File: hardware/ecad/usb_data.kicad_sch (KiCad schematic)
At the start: 0 parts

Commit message: finsihed 6/7 sheets, usb_data needs work. Some warnings to be dealt with aswell but no hard errors.
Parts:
- added C19: 100nF, Capacitor_SMD:C_01005_0402Metric, symbol Device:C
- added U6: TS3USB30EDGSR, Package_SO:TSSOP-10_3x3mm_P0.5mm, symbol Interface_USB:TS3USB30EDGSR
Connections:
- new net GND: C19.2, U6.5 (GND)
- new net MODE_SEL: U6.1 (S), U6.9 (~{OE})
- new net SYS_3V3: C19.1, U6.10 (VCC)
- new net USB_D+_ESP: U6.2 (D1+)
- new net USB_D+_KBD: U6.4 (D+)
- new net USB_D+_UP: U6.3 (D2+)
- new net USB_D-_ESP: U6.8 (D1-)
- new net USB_D-_KBD: U6.6 (D-)
- new net USB_D-_UP: U6.7 (D2-)
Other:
- company: (none) -> āvega sytems

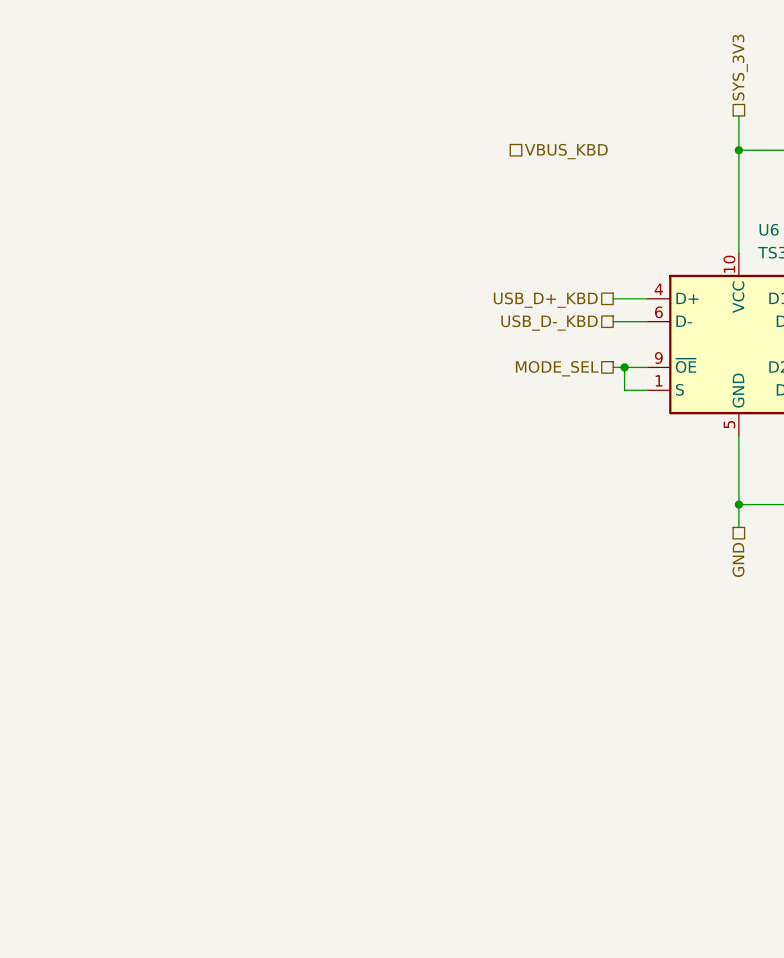
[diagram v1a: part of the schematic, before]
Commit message: feat: complete schematic design for midi2BLE v1
- Add 7-sheet hierarchical schematic covering full system architecture
- Power sheet: BQ24079RGTT charger, TPS62162DSG 3.3V buck, TLV61047DDC
  5V boost, PRTR5V0U2X ESD protection, USB-C receptacle with CC resistors
- ESP32-S3 sheet: WROOM-1-N8R2 module, UART header, boot/reset buttons,
  MODE_SEL debounce circuit, BAT_SENSE ADC input
- OLED UI sheet: SPI SSD1306 connector (GPIO35/36/10/9/8)
- Battery sense sheet: resistor divider for ADC1 battery voltage monitoring
- VBUS switching sheet: TPS2116DRL power mux for BOOST_5V/VBUS_IN selection
- USB data sheet: TS3USB30EDGSR USB 2.0 mux, keyboard USB-B connector,
  PRTR5V0U2X ESD protection on keyboard data lines
- Fix OLED from I2C to SPI, reassign GPIO11/12 away from octal flash
- Fix BQ24079 TS pin from VBUS_IN to 10k resistor to GND
- Set ISET=590R (1.5A charge), ILIM=1k (1.55A input limit) for 2500-3000mAh LiPo
- Pass ERC with 0 errors, 0 warnings (6 ignored: BQ24079 symbol quirks)
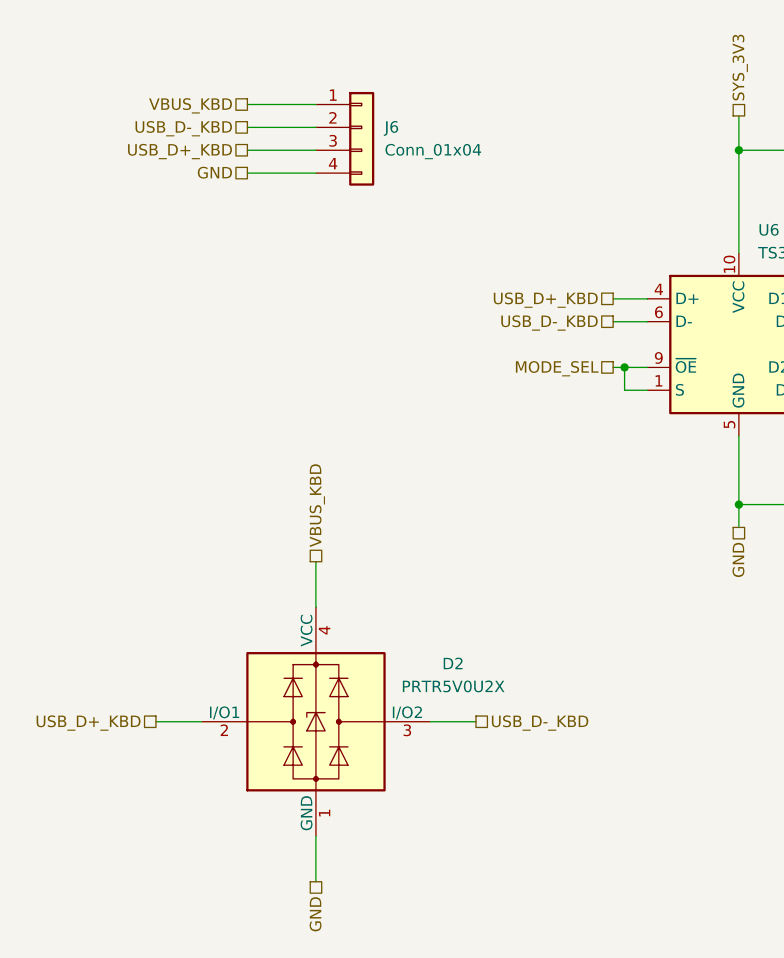
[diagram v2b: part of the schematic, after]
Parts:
- added D2: PRTR5V0U2X, Package_TO_SOT_SMD:SOT-143, symbol Power_Protection:PRTR5V0U2X
- added J6: Conn_01x04, Connector_JST:JST_PH_B4B-PH-K_1x04_P2.00mm_Vertical, symbol Connector_Generic:Conn_01x04
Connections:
- net GND: now also D2.1 (GND), J6.4 (Pin_4)
- net USB_D+_KBD: now also D2.2 (I/O1), J6.3 (Pin_3)
- net USB_D-_KBD: now also D2.3 (I/O2), J6.2 (Pin_2)
- net VBUS_KBD: now also D2.4 (VCC), J6.1 (Pin_1)

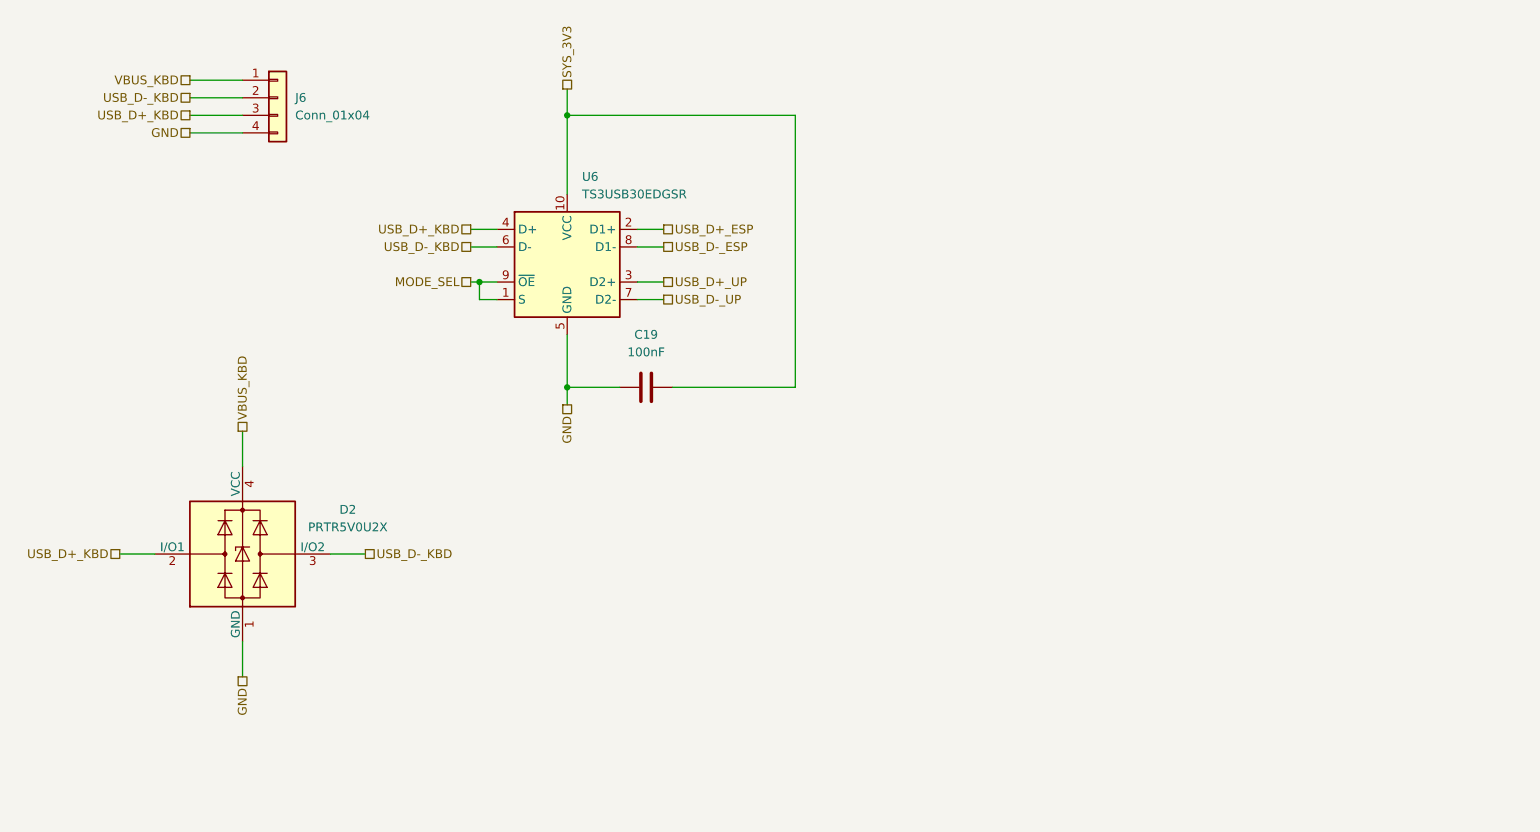
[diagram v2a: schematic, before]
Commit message: Updated schematics and added printed pdf
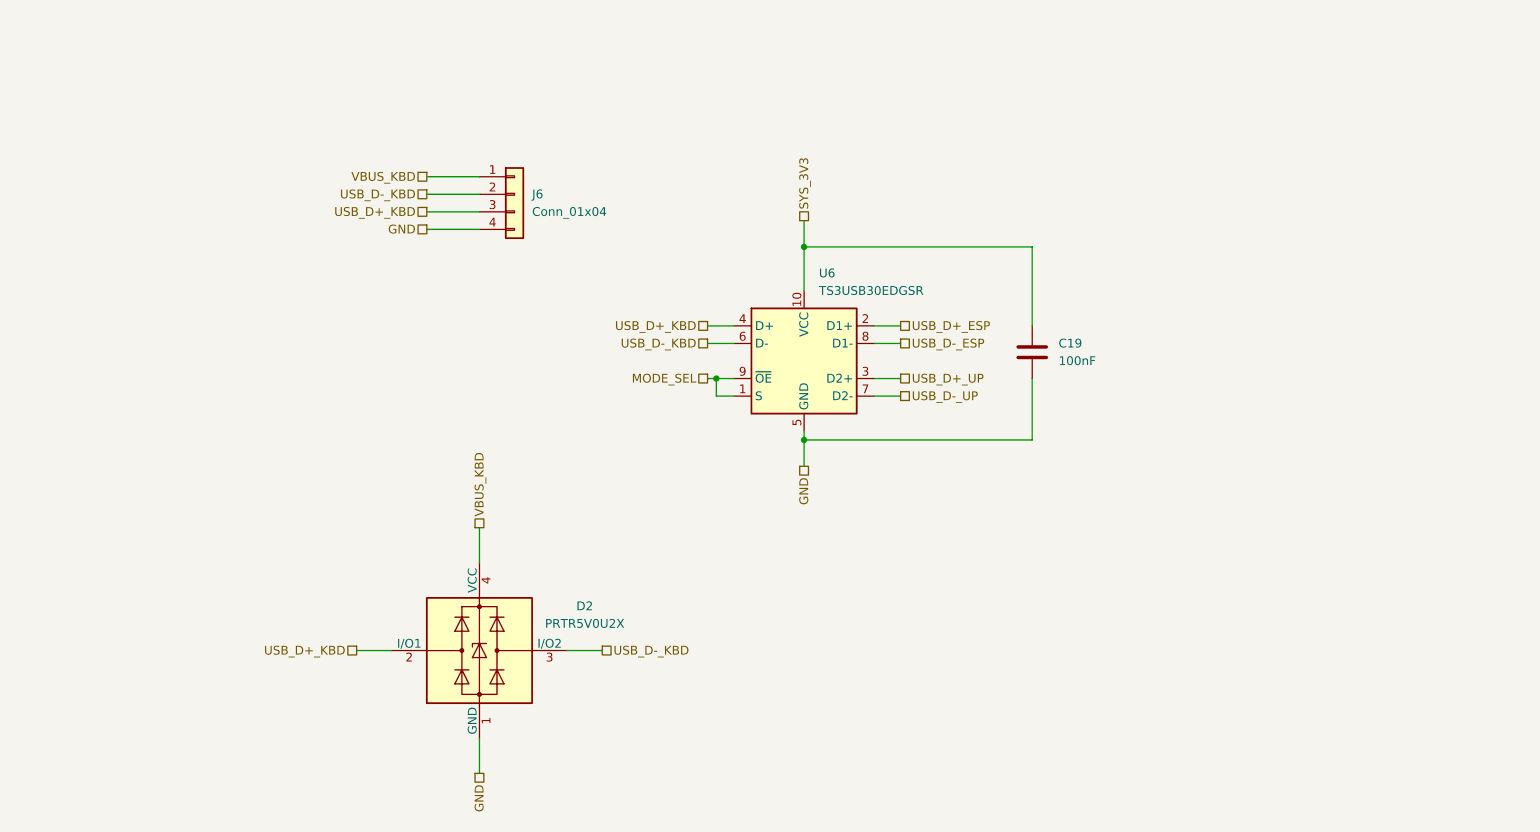
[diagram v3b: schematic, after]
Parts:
- C19: footprint Capacitor_SMD:C_01005_0402Metric -> Capacitor_SMD:C_0402_1005Metric
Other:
- title: (none) -> midi2BLE_USB_data
- moved on the sheet: D2, J6, U6

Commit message: docs(hardware): update ecad README to reflect completed schematic and PCB — PCB IS DONE!!!
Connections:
- net USB_D+_ESP renamed USB_ESP+
- net USB_D+_KBD renamed USB_KBD+
- net USB_KBD+: now also J6.2 (Pin_2); no longer J6.3 (Pin_3)
- net USB_D+_UP renamed USB_UP+
- net USB_D-_ESP renamed USB_ESP-
- net USB_D-_KBD renamed USB_KBD-
- net USB_KBD-: now also J6.3 (Pin_3); no longer J6.2 (Pin_2)
- net USB_D-_UP renamed USB_UP-
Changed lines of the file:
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@@
 		)
 	)
-	(hierarchical_label "USB_D+_KBD"
-		(shape passive)
-		(at 114.3 59.69 180)
-		(effects
-			(font
-				(size 1.27 1.27)
-			)
-			(justify right)
-		)
-	)
-	(hierarchical_label "USB_D-_ESP"
+	(hierarchical_label "USB_ESP-"
 		(shape passive)
 		(at 182.88 78.74 0)
@@
 		)
 	)
-	(hierarchical_label "USB_D-_KBD"
-		(shape passive)
-		(at 114.3 57.15 180)
-		(effects
-			(font
-				(size 1.27 1.27)
-			)
-			(justify right)
-		)
-	)
-	(hierarchical_label "USB_D+_KBD"
+	(hierarchical_label "USB_KBD+"
 		(shape passive)
 		(at 154.94 76.2 180)
@@
 		)
 	)
-	(hierarchical_label "USB_D-_KBD"
+	(hierarchical_label "USB_KBD-"
+		(shape passive)
+		(at 114.3 59.69 180)
+		(effects
+			(font
+				(size 1.27 1.27)
+			)
+			(justify right)
+		)
+	)
+	(hierarchical_label "USB_KBD-"
 		(shape passive)
 		(at 154.94 78.74 180)
@@
 		)
 	)
-	(hierarchical_label "USB_D-_KBD"
+	(hierarchical_label "USB_KBD-"
 		(shape passive)
 		(at 139.7 123.19 0)
@@
 		)
 	)
-	(hierarchical_label "USB_D+_KBD"
+	(hierarchical_label "USB_KBD+"
 		(shape passive)
 		(at 104.14 123.19 180)
@@
 		)
 	)
-	(hierarchical_label "USB_D+_UP"
+	(hierarchical_label "USB_UP+"
 		(shape passive)
 		(at 182.88 83.82 0)
@@
 		)
 	)
-	(hierarchical_label "USB_D-_UP"
+	(hierarchical_label "USB_UP-"
 		(shape passive)
 		(at 182.88 86.36 0)
@@
 		)
 	)
-	(hierarchical_label "USB_D+_ESP"
+	(hierarchical_label "USB_KBD+"
+		(shape passive)
+		(at 114.3 57.15 180)
+		(effects
+			(font
+				(size 1.27 1.27)
+			)
+			(justify right)
+		)
+	)
+	(hierarchical_label "USB_ESP+"
 		(shape passive)
 		(at 182.88 76.2 0)

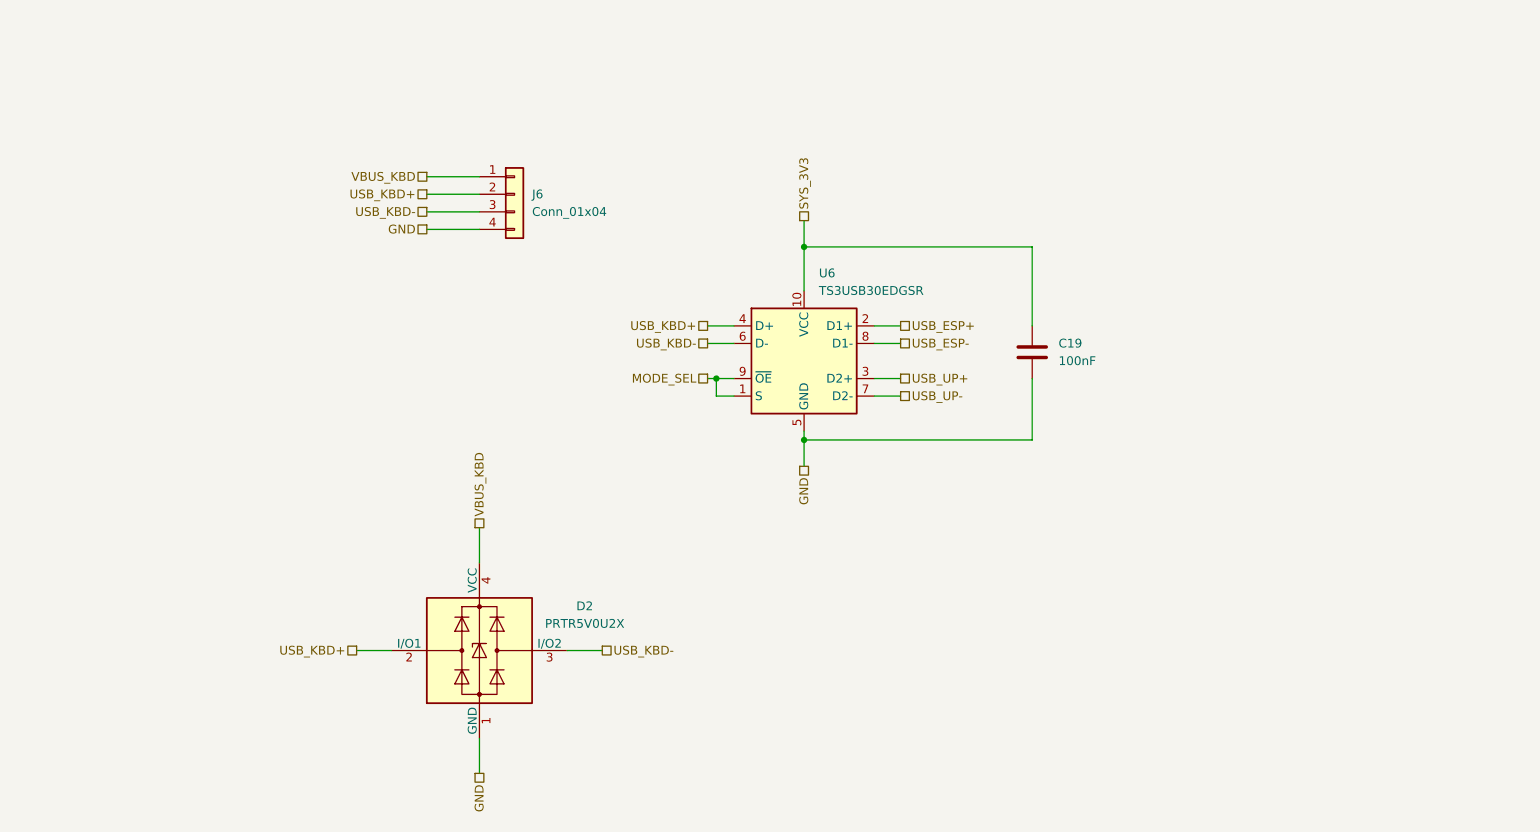
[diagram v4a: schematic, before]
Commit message: fix: resolve fatal power and USB switching errors
Replace TLV61047 boost converter with MT3608; add SS14 catch diode, 4.7µH inductor, and correct FB divider (180kΩ/51kΩ) for 5V output
Fix TPS62162DSG EN circular dependency; connect directly to U1_OUT
Fix TPS62162DSG FB pin; disconnect from SYS_3V3 and tie to GND
Fix TPS2116 power mux; remove series resistor on VIN1, add correct PR1 divider (100kΩ/27kΩ), tie MODE to VIN1 for priority mode
Fix TS3USB30E OE pin; tie directly to GND to keep switch always enabled
Add PGOOD pull-up resistor (10kΩ) to SYS_3V3 on BQ24079
Change ISET resistor from 590Ω to 680Ω for 1.3A charge current
Remove unnecessary R5 (10kΩ VBUS_IN to GND bleed resistor)
Add USB_STATUS net from TPS2116 ST pin to ESP32 IO38
Add PWR_FLAG to BOOST_5V and U1_OUT nets
Fix U1_PGOOD net label placement; separate from SYS_3V3 pull-up node
Add documentation boxes and truth tables to power and USB switching pages
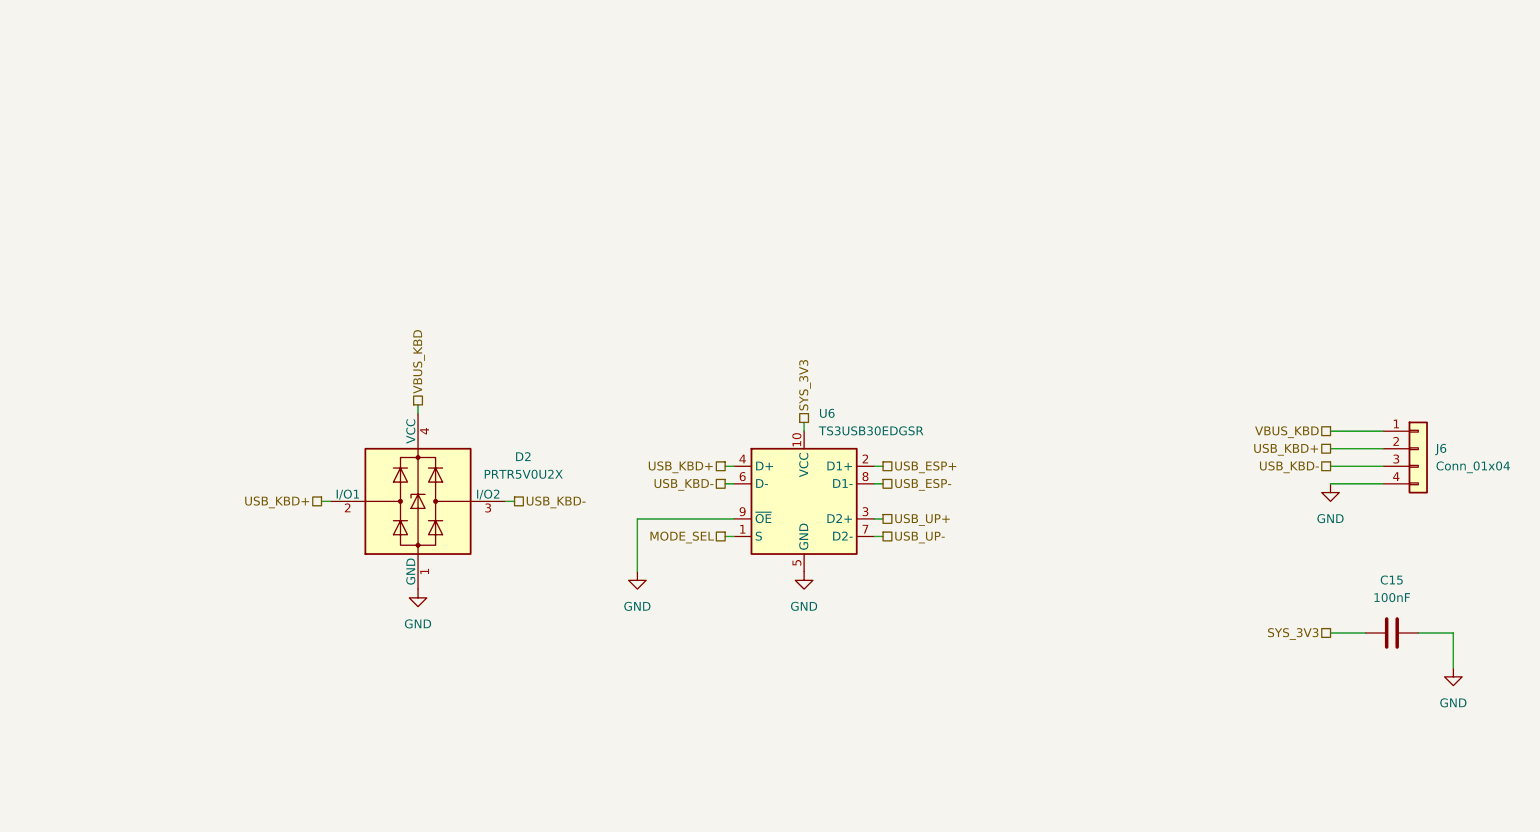
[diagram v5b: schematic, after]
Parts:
- removed C19: 100nF, Capacitor_SMD:C_0402_1005Metric, symbol Device:C
- added C15: 100nF, Capacitor_SMD:C_0402_1005Metric, symbol Device:C
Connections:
- net GND: now also U6.9 (~{OE}), C15.1
- net MODE_SEL: no longer U6.9 (~{OE})
- net SYS_3V3: now also C15.2
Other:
- moved on the sheet: D2, J6, U6

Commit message: Fixed minor errors and smaller issues withing schematics, moved v1 pcb and specific projet artifacts to archive. Produced PDF of full schematic
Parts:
- C15: footprint Capacitor_SMD:C_0402_1005Metric -> Capacitor_SMD:C_0603_1608Metric
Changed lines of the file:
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@@
 	(title_block
 		(title "midi2BLE_USB_data")
-		(date "2026-04-14")
-		(rev "1")
+		(date "2026-05-16")
+		(rev "2")
 		(company "āvega sytems")
 	)
@@
 			)
 		)
-		(property "Footprint" "Capacitor_SMD:C_0402_1005Metric"
+		(property "Footprint" "Capacitor_SMD:C_0603_1608Metric"
 			(at 250.19 121.6152 0)
 			(hide yes)
